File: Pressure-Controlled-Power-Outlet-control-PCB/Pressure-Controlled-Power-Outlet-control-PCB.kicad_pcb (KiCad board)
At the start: 4 copper layers, 100.3 x 100.3 mm, 47 parts, among them J1 Analog water pressure sensor 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, J2 1017514, J3 I2C0 Connector, J4 SPI1 Connector, J5 FanA 5V/24V, J6 FanB 5V/24V, K1 T9GV5L24-24, K2 T9GV5L24-24, M1 Fan_4pin, M2 Fan_4pin, Q1 2N3906, Q2 IRF540N, Q3 IRF540N, Q4 2N3906, Q5 2N3904, Q6 2N3904, Q7 2N3904, Q8 2N3904, U1 Pico, U2 LM324, U3 LF50_TO220

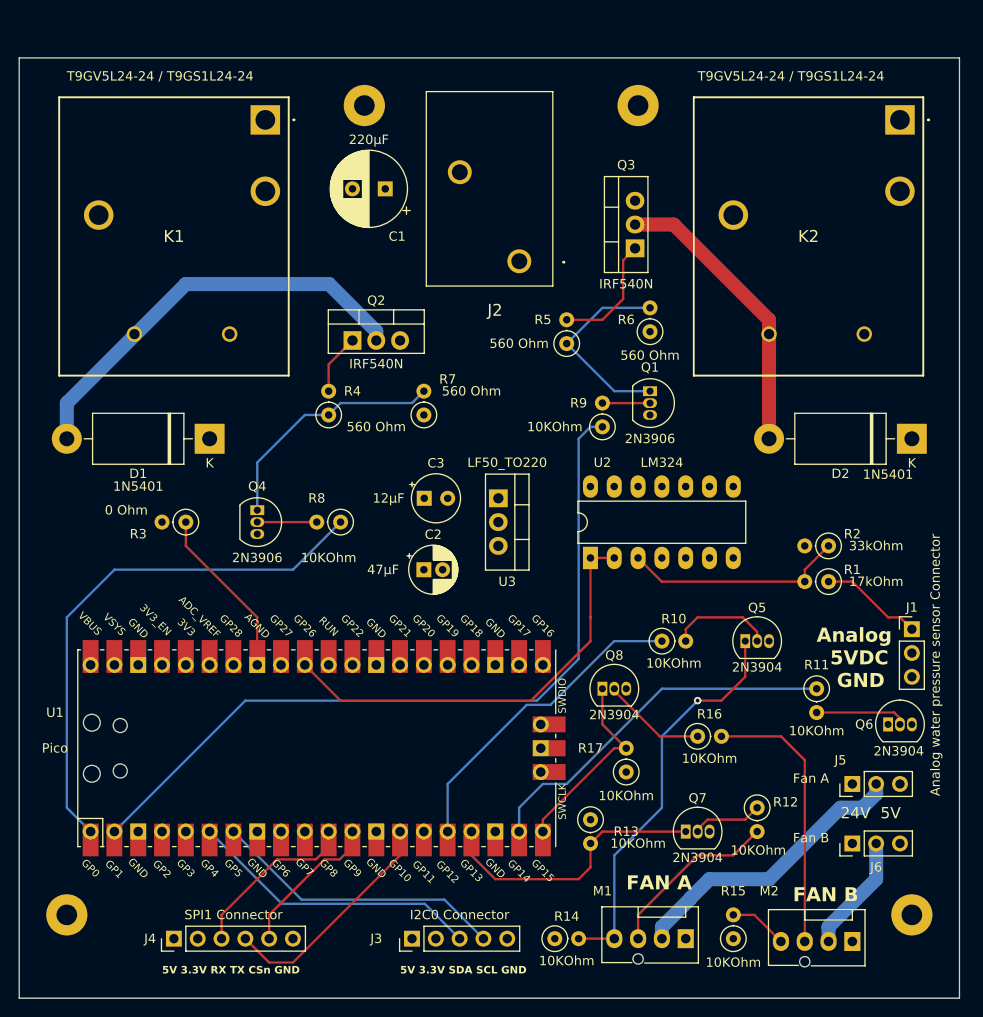
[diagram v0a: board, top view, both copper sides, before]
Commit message: upgraded diodes to 1n5405 from 1n5401
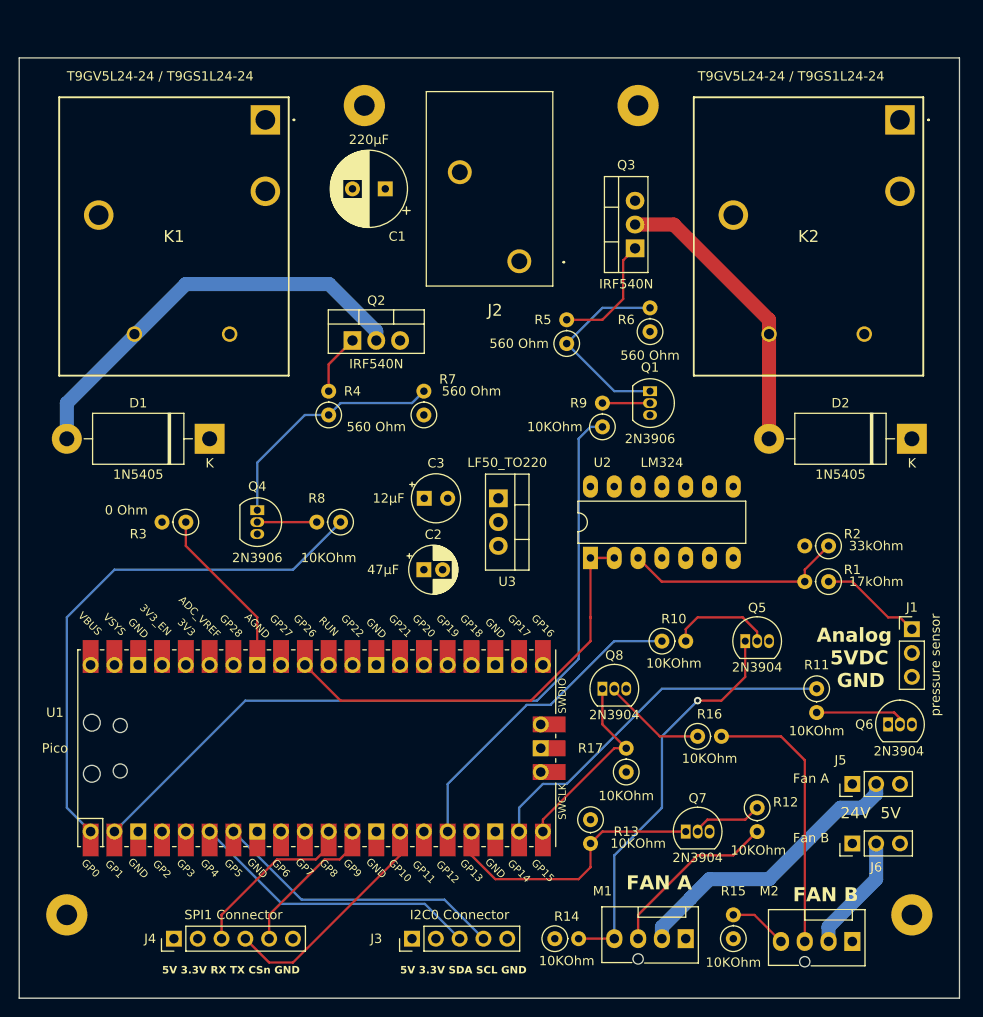
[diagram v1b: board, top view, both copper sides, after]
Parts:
- D1, D2: value 1N5401 -> 1N5405
- J1: value Analog water pressure sensor Connector -> pressure sensor

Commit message: finished the through hole version of the board going to make a smd version for pick and place
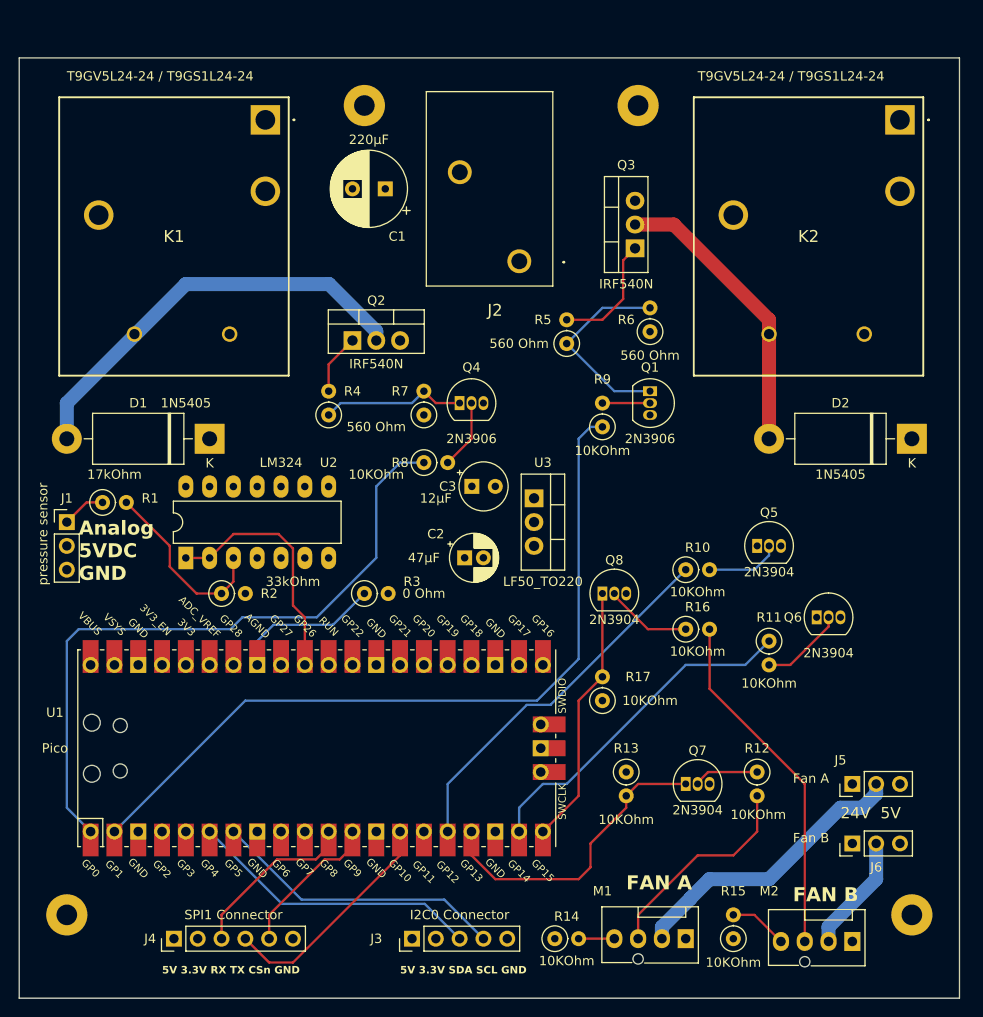
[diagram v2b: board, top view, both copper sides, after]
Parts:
- moved J1 90.9 mm to (91.4, 105.4)
- moved R1 77.9 mm to (95.2, 103.3), turned to 0 degrees
- moved R2 65.0 mm to (108.0, 113.0), turned to 0 degrees
- moved U2 43.2 mm to (104.1, 109.2)
- moved Q4 24.4 mm to (133.3, 92.7), turned to 0 degrees
- moved R3 20.5 mm to (123.2, 113.0), turned to 0 degrees
- moved Q6 13.7 mm to (171.4, 115.6)
- moved R16 11.5 mm to (157.5, 116.8)
- moved R8 10.9 mm to (129.5, 99.1), turned to 0 degrees
- moved Q5 10.2 mm to (165.1, 108.0)
- moved Q8 10.2 mm to (148.6, 113.0)
- moved R17 8.03 mm to (148.6, 124.5)
- moved R10 8.03 mm to (157.5, 110.5)
- moved R11 7.18 mm to (166.4, 118.1)
- moved R13 6.35 mm to (151.1, 132.1)
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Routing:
- net /ADC0: track 46.1 -> 26.1 mm
- net +5V: track 20.9 -> 37.4 mm
- net /Activate_Live: track 57.3 -> 71.8 mm
- net Net-(Q4-E): track 26.0 -> 15.5 mm
- net Net-(M1-PWM): track 42.8 -> 52.0 mm, vias 1 -> 0
- net Net-(M2-Tacho): track 29.3 -> 37.5 mm
- net /FanB_Tac: track 20.7 -> 28.0 mm
- net +3.3V: track 133.7 -> 140.9 mm
- net Net-(M2-PWM): track 34.9 -> 41.7 mm
- net /Water Pressure 5V: track 11.0 -> 4.68 mm
- net /FanA_PWM: track 34.3 -> 39.9 mm
- net Net-(U2A-+): track 23.7 -> 19.8 mm
- net Net-(M1-Tacho): track 18.9 -> 22.7 mm
- net Net-(Q5-B): track 11.1 -> 7.99 mm
- net /FanB_PWM: track 39.6 -> 36.6 mm
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
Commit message: added better longer lasting caps
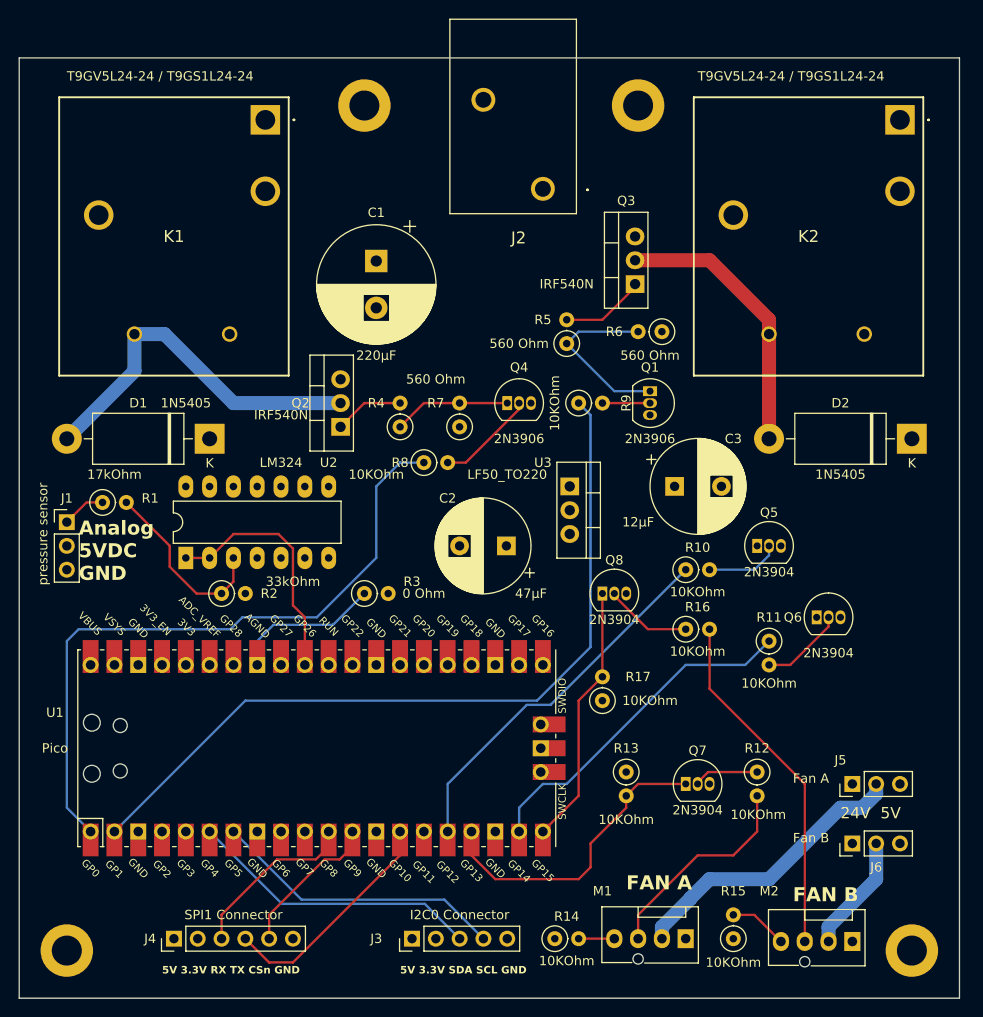
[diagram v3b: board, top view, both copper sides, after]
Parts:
- C1: footprint Capacitor_THT:CP_Radial_D8.0mm_P3.50mm -> Capacitor_THT:CP_Radial_D12.5mm_P5.00mm
- C2: footprint Capacitor_THT:CP_Radial_D5.0mm_P2.00mm -> Capacitor_THT:CP_Radial_D10.0mm_P5.00mm
- C3: footprint Capacitor_THT:CP_Radial_Tantal_D5.0mm_P2.50mm -> Capacitor_THT:CP_Radial_D10.0mm_P5.00mm
- H1, H2, H3, H4: footprint MountingHole:MountingHole_2.2mm_M2_Pad -> MountingHole:MountingHole_3.2mm_M3_DIN965_Pad
- moved C3 21.6 mm to (156.3, 101.6)
- moved Q2 9.30 mm to (120.7, 95.2), turned to 90 degrees
- moved J2 8.12 mm to (142.2, 69.8)
- moved C1 7.76 mm to (124.5, 77.5), turned to -90 degrees
- moved R4 7.73 mm to (127.0, 95.2)
- moved Q4 5.08 mm to (138.4, 92.7)
- moved C2 4.64 mm to (138.3, 108.0), turned to 180 degrees
- moved U3 4.02 mm to (145.1, 101.6)
- moved R7 4.02 mm to (133.3, 95.2)
- moved H1 3.81 mm to (181.6, 151.1)
- moved H2 3.81 mm to (91.4, 151.1)
- moved Q3 3.81 mm to (152.1, 80.0)
- moved R9 3.59 mm to (146.1, 92.7), turned to 0 degrees
- moved R6 1.27 mm to (154.9, 85.1), turned to 180 degrees
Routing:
- net +5V: track 37.4 -> 29.2 mm
- net Net-(D1-A): track 45.2 -> 39.2 mm
- net Net-(Q3-G): track 12.9 -> 9.06 mm
- net Net-(Q4-B): track 7.40 -> 10.6 mm
- net Net-(Q4-E): track 15.5 -> 12.5 mm
- net Net-(Q1-E): track 21.5 -> 19.1 mm
- net /Activate_Neutral: track 83.7 -> 85.5 mm
- net Net-(D2-A): track 31.2 -> 29.6 mm
- net Net-(Q2-G): track 6.46 -> 7.40 mm

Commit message: hopefully done this PCB
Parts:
- H1, H2, H3, H4: footprint MountingHole:MountingHole_3.2mm_M3_DIN965_Pad -> MountingHole:MountingHole_4.3mm_M4_Pad
- moved M2 2.54 mm to (172.7, 150.2)
- moved J2 2.52 mm to (139.7, 69.8)
- moved H3 1.80 mm to (151.1, 62.2)
- moved H1 1.80 mm to (180.3, 149.9)
- moved R15 1.80 mm to (161.3, 151.1)
- moved H2 1.80 mm to (92.7, 149.9)
- moved H4 1.27 mm to (123.2, 62.2)
- moved C1 1.13 mm to (124.5, 76.4)
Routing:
- net Net-(D1-A): track 39.2 -> 37.6 mm
- net Net-(M2-Tacho): track 37.5 -> 36.5 mm
- net /FanB_Power: track 12.6 -> 13.6 mm
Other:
- board text added: "24V GND 5V"
- board text added: "Pressure Controlled Power Outlet control PCB 2024-07-19 V1.3.1 By Brian Banas"
- board text removed: "Pressure Controlled Power Outlet control PCB 2024-07-19 V1.2.3 By Brian Banas"

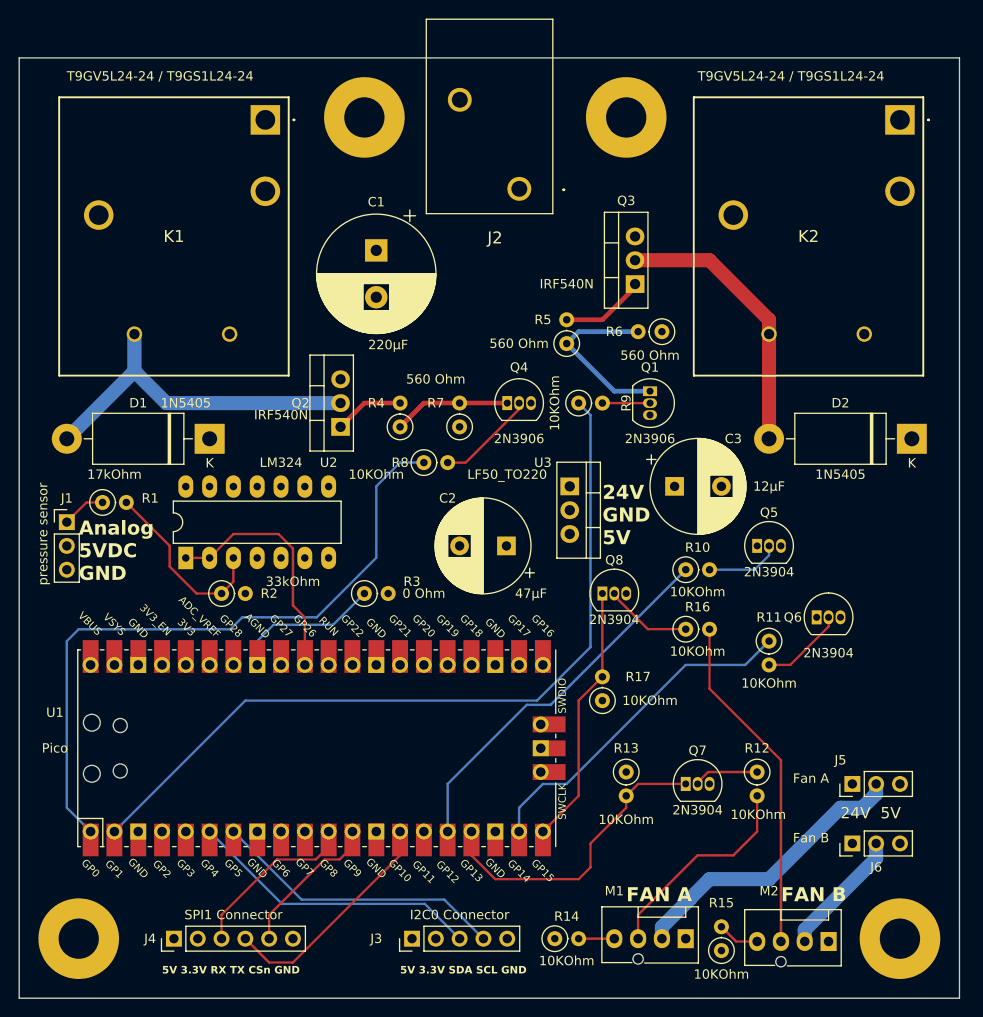
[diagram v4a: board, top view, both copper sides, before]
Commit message: updated 220µF cap
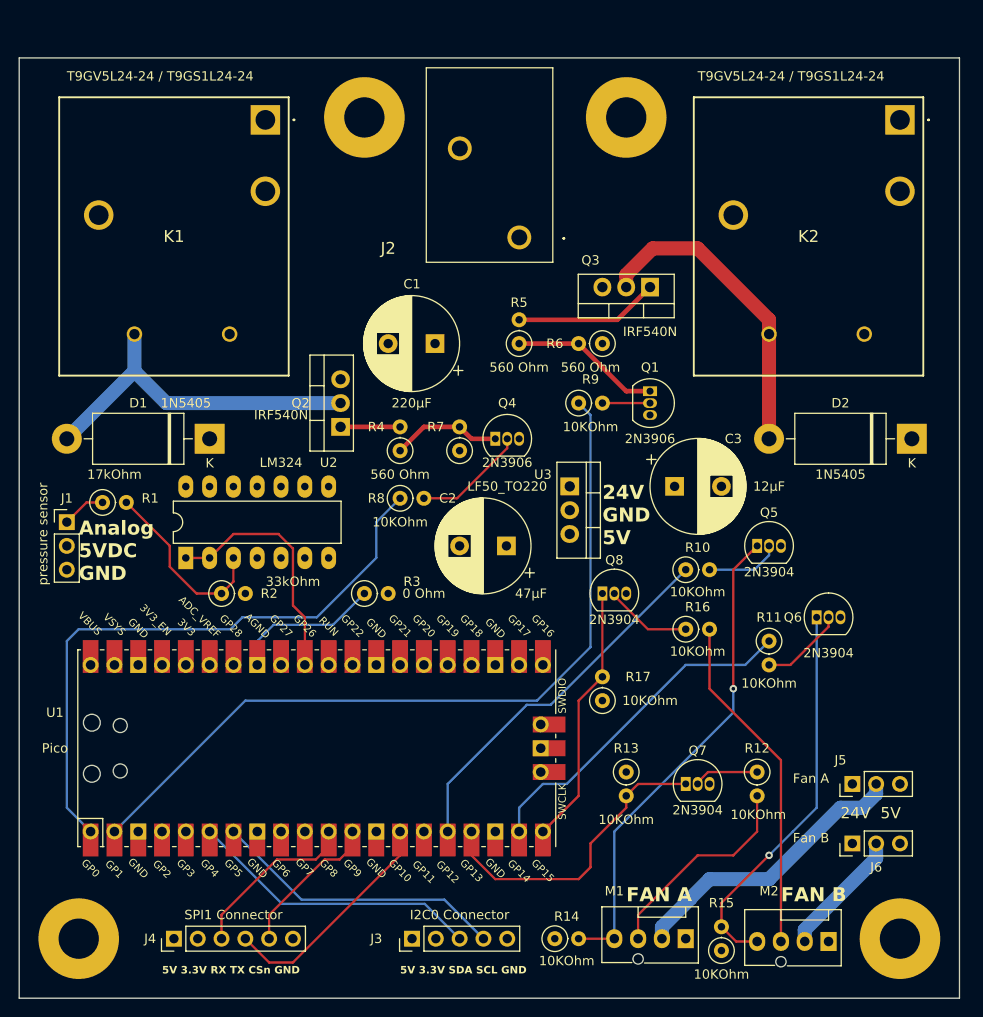
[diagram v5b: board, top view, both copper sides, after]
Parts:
- C1: footprint Capacitor_THT:CP_Radial_D12.5mm_P5.00mm -> Capacitor_THT:CP_Radial_D10.0mm_P5.00mm
- moved C1 11.8 mm to (130.7, 86.4), turned to 180 degrees
- moved R6 6.48 mm to (148.6, 86.4)
- moved J2 5.19 mm to (139.7, 75.0)
- moved R5 5.08 mm to (139.7, 86.4)
- moved R8 4.58 mm to (127.0, 102.9)
- moved Q4 4.02 mm to (137.2, 96.5)
- moved R4 2.54 mm to (127.0, 97.8)
- moved R7 2.54 mm to (133.3, 97.8)
- moved Q3 1.63 mm to (153.7, 80.3), turned to 180 degrees
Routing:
- net Net-(Q3-G): track 8.74 -> 15.4 mm
- net /Activate_Live: track 71.8 -> 65.5 mm
- net Net-(D2-A): track 29.6 -> 33.6 mm
- net +5V: track 29.2 -> 25.9 mm
- net Net-(Q1-E): track 19.1 -> 16.1 mm
- net Net-(Q4-B): track 10.6 -> 12.1 mm
- net Net-(Q2-G): track 7.40 -> 6.35 mm
- net Net-(Q4-E): track 12.5 -> 11.7 mm
- net Net-(M1-PWM): vias 0 -> 1
- net Net-(M2-PWM): vias 0 -> 1

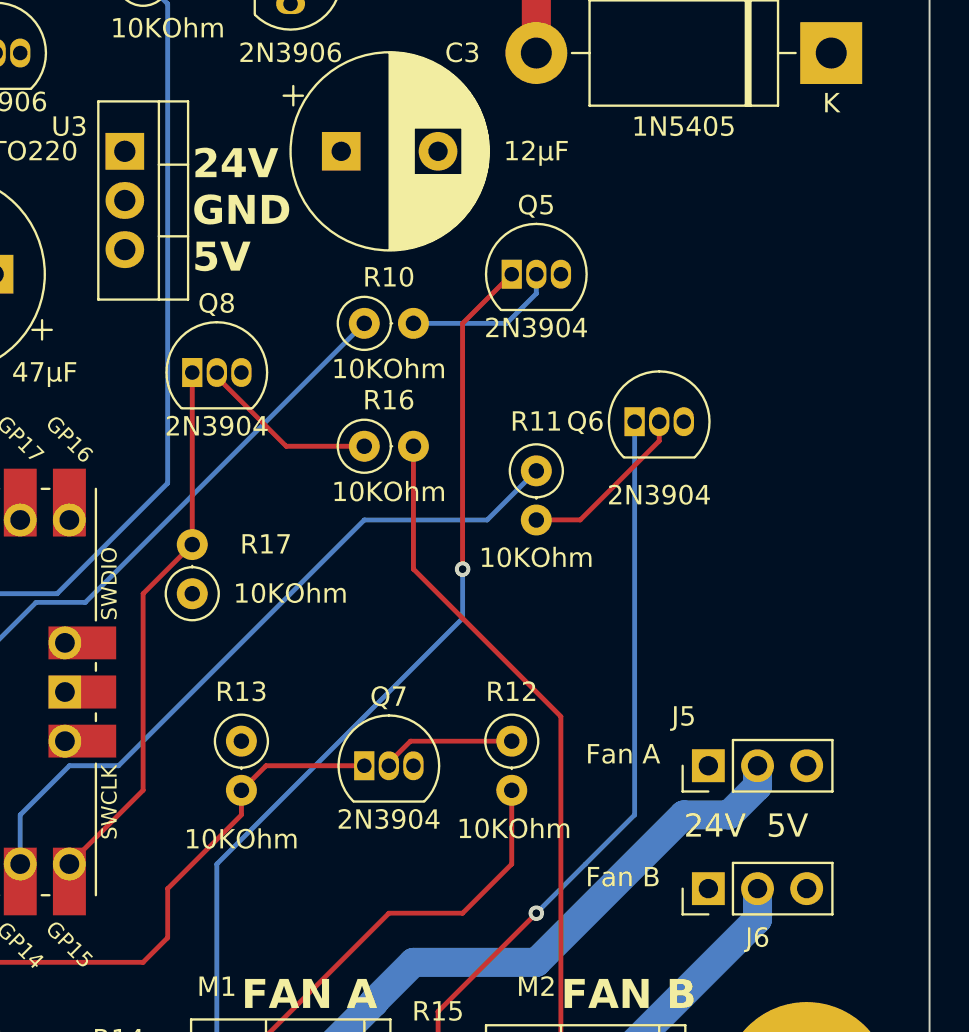
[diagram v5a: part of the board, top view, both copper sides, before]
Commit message: changed 24V fan power to 12V
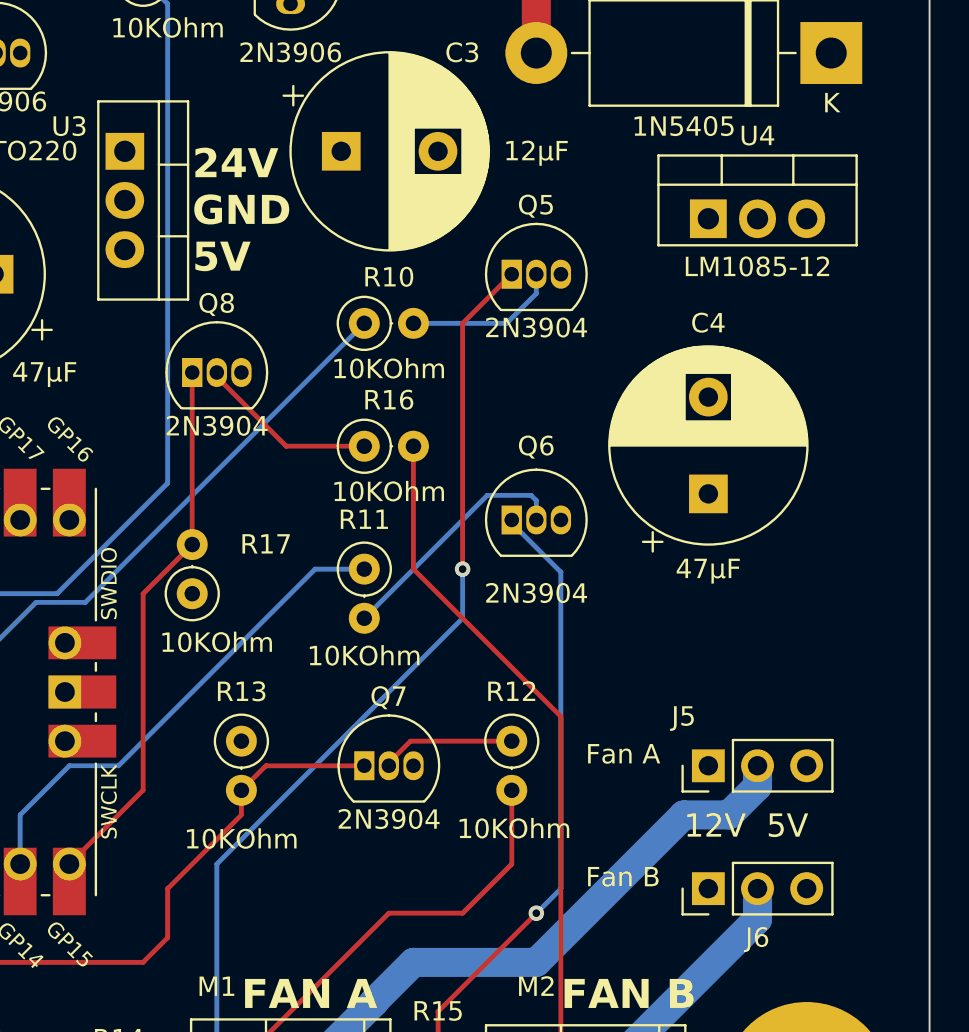
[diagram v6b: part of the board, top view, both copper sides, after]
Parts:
- added C4: 47µF, Capacitor_THT:CP_Radial_D10.0mm_P5.00mm, F.Cu at (175.3, 119.3)
- added U4: LM1085-12, Package_TO_SOT_THT:TO-220-3_Vertical, F.Cu at (175.3, 105.1)
- J5: value FanA 5V/24V -> FanA 5V/12V
- J6: value FanB 5V/24V -> FanB 5V/12V
- moved R11 10.2 mm to (157.5, 123.2)
- moved Q6 8.13 mm to (165.1, 120.7)
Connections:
- J5 pad 1: +24V -> +12V
- J6 pad 1: +24V -> +12V
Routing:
- net +24V: track 45.8 -> 0.00 mm
- net +12V: track 0.00 -> 35.7 mm
- net /FanB_PWM: track 36.6 -> 25.6 mm
- net Net-(M2-PWM): track 41.7 -> 36.1 mm
- net Net-(Q6-B): track 9.04 -> 12.6 mm
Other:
- board text added: "12V 5V"
- board text removed: "24V 5V"
